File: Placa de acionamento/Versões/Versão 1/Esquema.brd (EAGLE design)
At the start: 73.6 x 58.5 mm, 23 parts, among them Q1 IRF540, Q2 IRF540, Q3 IRF540

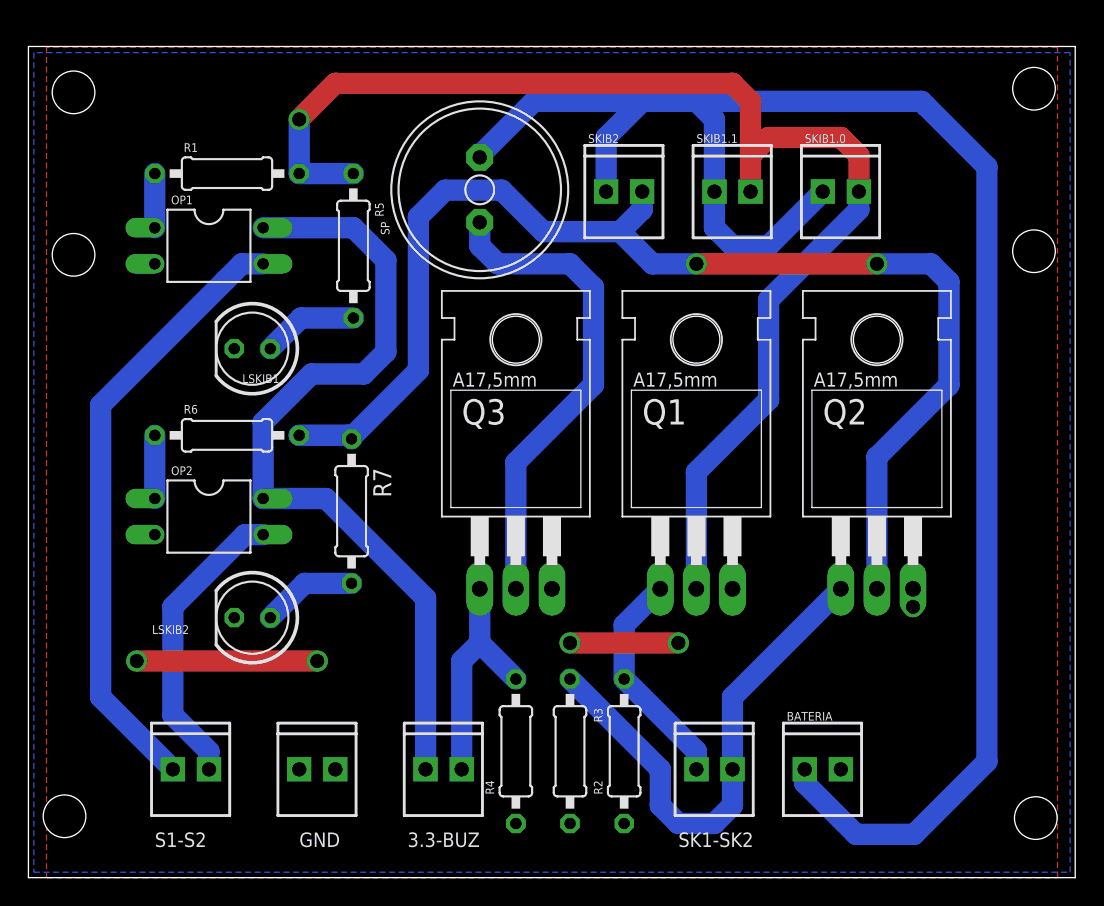
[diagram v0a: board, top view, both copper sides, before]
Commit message: mudanças na placa de processamento
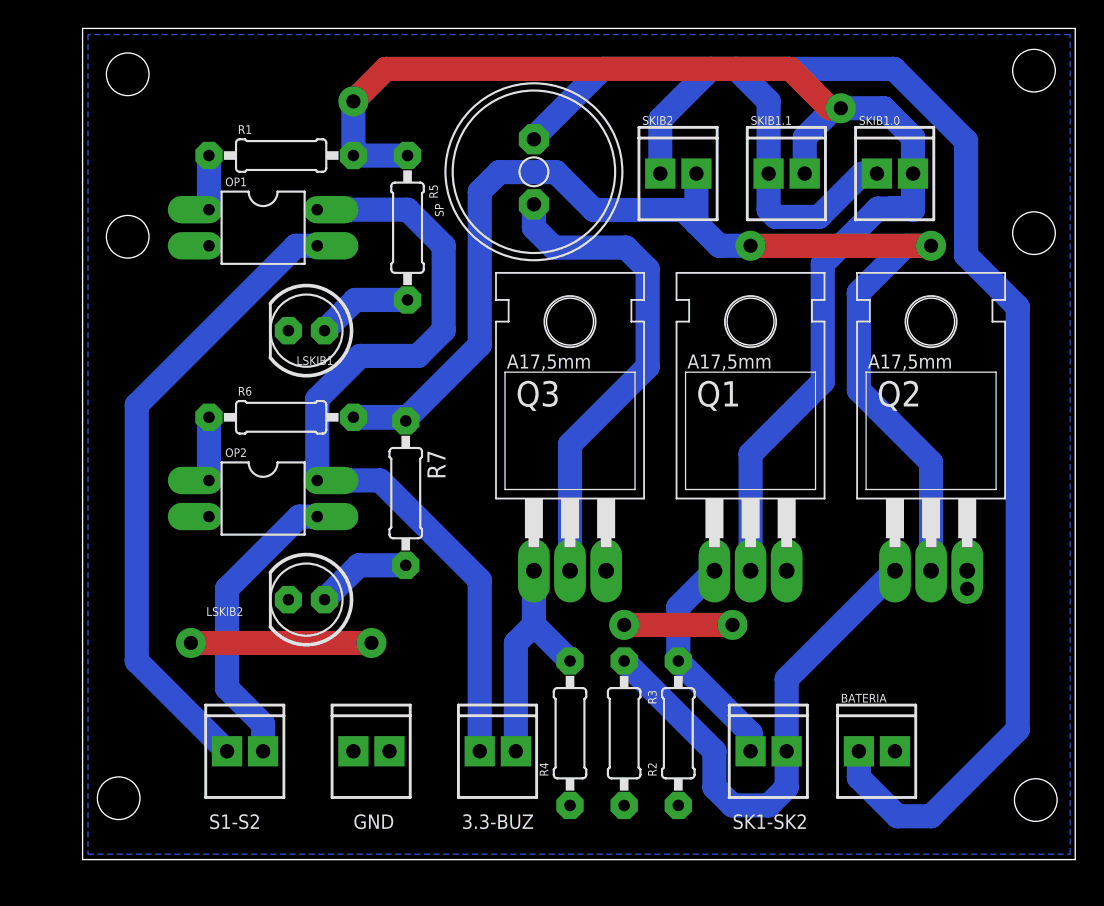
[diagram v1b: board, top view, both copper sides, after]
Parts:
- moved Q1 4.02 mm to (47.0, 26.7)
- moved 3.3-BUZ 4.02 mm to (27.9, 7.62)
- moved BATERIA 4.02 mm to (54.6, 7.62)
- moved R3 4.02 mm to (38.1, 8.89)
- moved SK1-SK2 4.02 mm to (47.0, 7.62)
- moved R1 4.02 mm to (14.0, 49.5)
- moved R7 4.02 mm to (22.7, 25.8)
- moved GND 4.02 mm to (19.1, 7.62)
- moved S1-S2 4.02 mm to (10.2, 7.62)
- moved SKIB1.0 4.02 mm to (55.9, 48.3)
- moved SKIB2 4.02 mm to (40.6, 48.3)
- moved OP1 4.02 mm to (12.7, 44.5)
- moved Q3 4.02 mm to (34.3, 26.7)
- moved R5 4.02 mm to (22.9, 44.5)
- moved R6 4.02 mm to (14.0, 31.1)
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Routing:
- net VCC: track 125.1 -> 123.0 mm
- net SKIB1_CONECTOR: track 91.2 -> 92.7 mm, vias 1 -> 2
- net SINAL_SKIB1: track 43.3 -> 44.3 mm
- net SKIB2_CONECTOR: track 92.8 -> 91.8 mm
- removed copper zone on layer 1, net GND
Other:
- board size 73.6 x 58.5 mm -> 69.8 x 58.5 mm
